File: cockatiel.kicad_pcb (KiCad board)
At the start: 4 copper layers, 38 parts, among them J1 Programmer, J10 LED1_EXT, J11 LED1_SEL, J12 LED0_EXT, J13 LED0_SEL, J14 I/O Debug, J15 MIC_P_BYPASS, J16 MIC_N_BYPASS, J17 MIC_P_SEL, J18 MIC_N_SEL, J19 Cox Box Mic In, J20 Cox Box Mic Out, J21 Microphone out, J22 Headset Socket, J3 DEBUG_UART, J4 RESET, J5 Magnetic connector, J6 PANEL_POWER_BUTTON (MFB), J7 Battery Connector, J8 LED2_EXT, J9 LED2_SEL, U1 F-3188_CSR8645

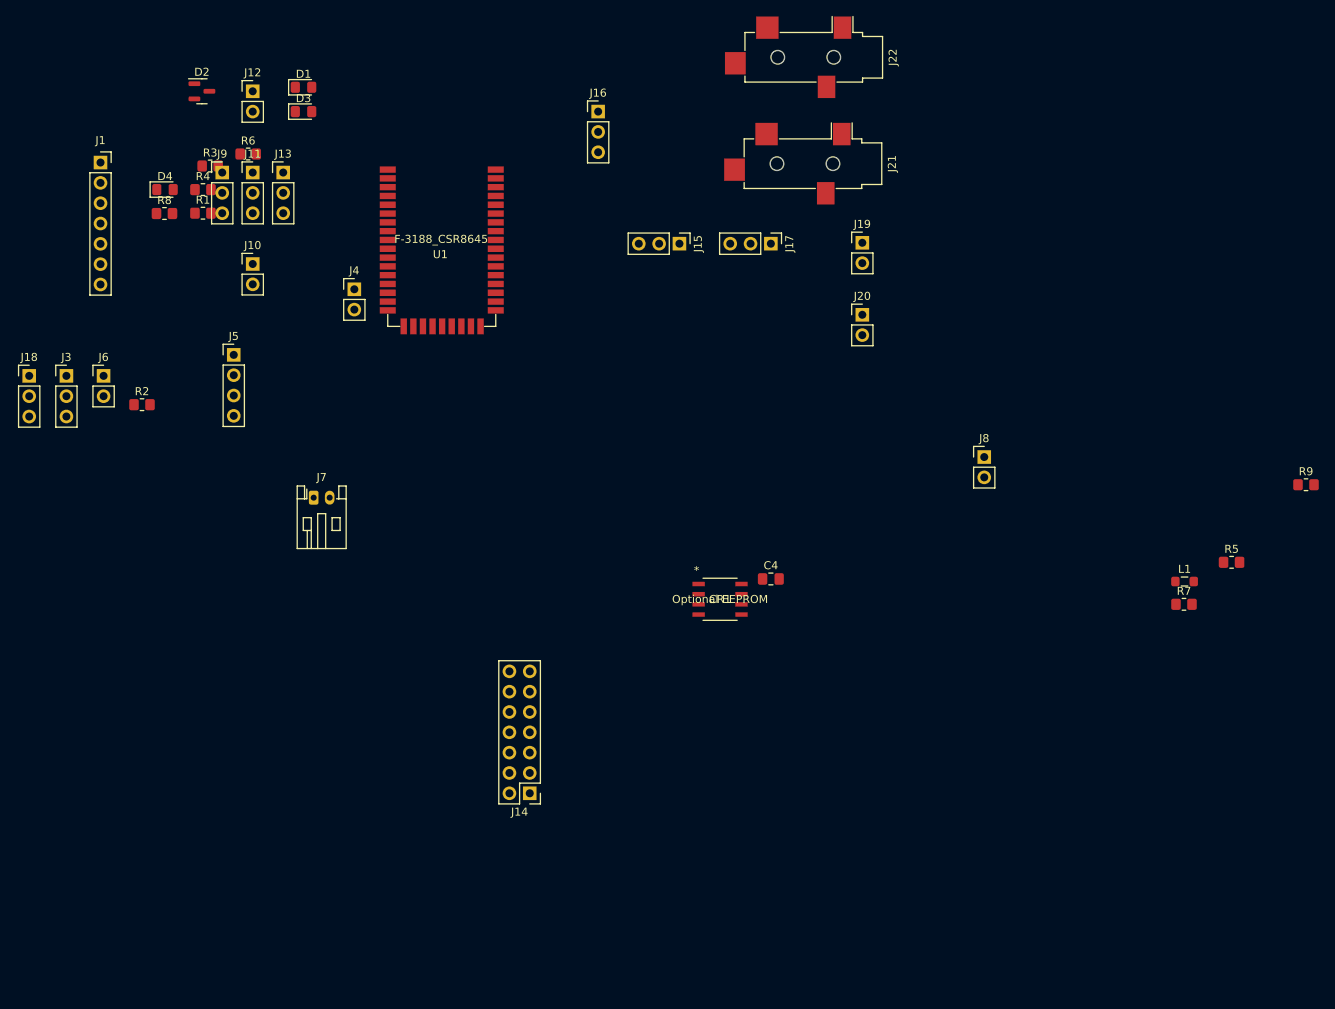
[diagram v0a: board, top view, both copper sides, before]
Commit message: WIP
1. Add transformer footprint.
2. PCB routing
3. Misc changes to re-add JLCPCB part numbers.
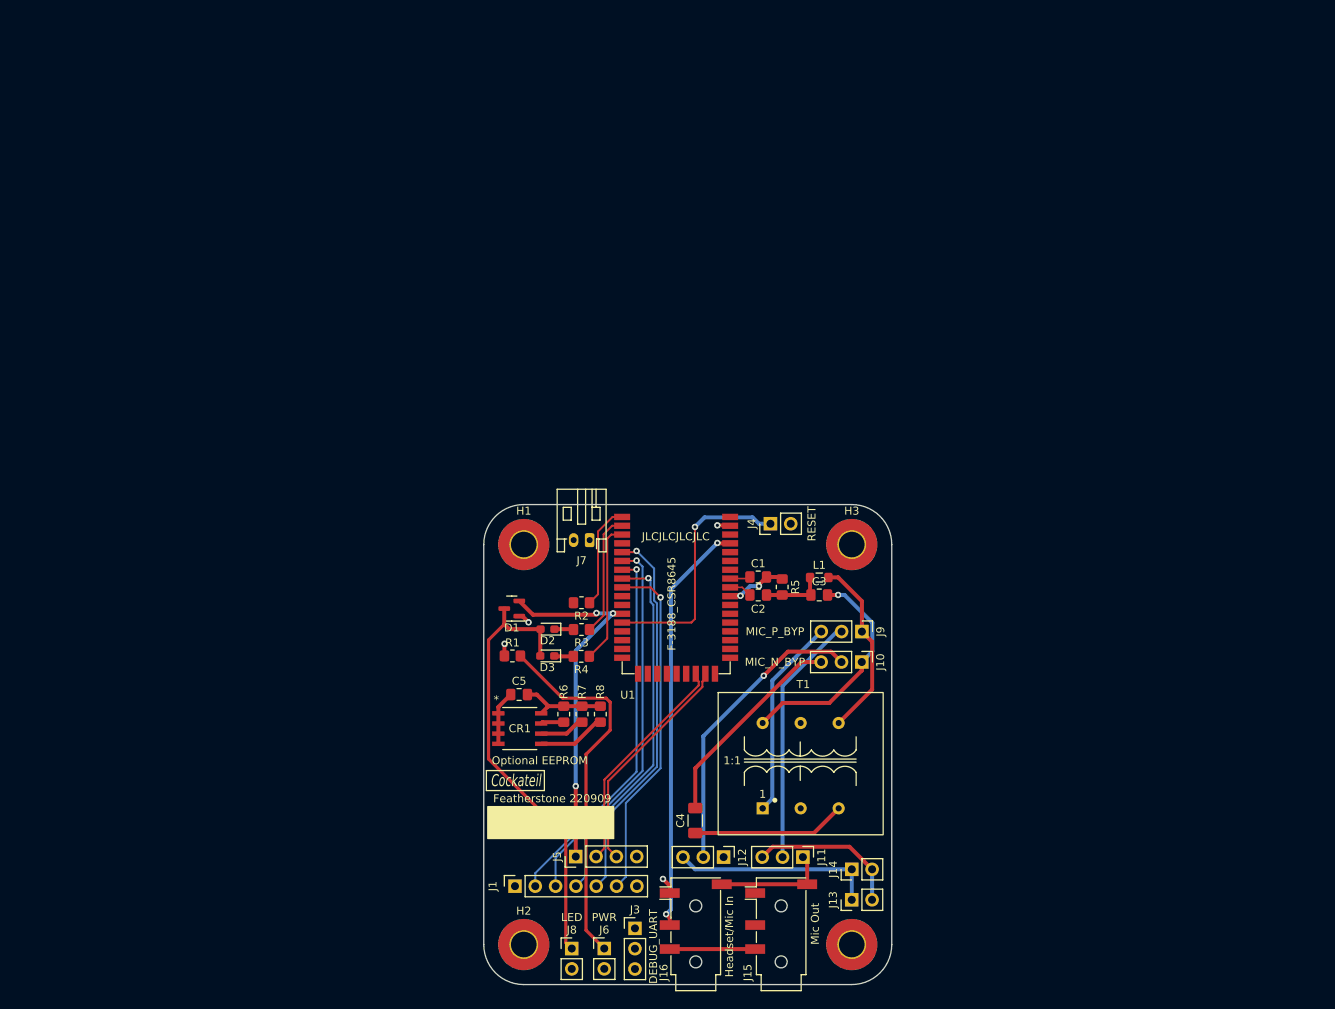
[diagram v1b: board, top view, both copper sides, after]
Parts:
- removed the D1 at (77.5, 52.8)
- removed the J10 at (71.1, 74.9)
- removed the J11 at (71.1, 63.5)
- removed the J12 at (71.1, 53.3)
- removed the J13 at (74.9, 63.5)
- removed the J14 at (105.8, 141.1)
- removed the J9 at (67.3, 63.5)
- removed the R2 at (57.3, 92.5)
- removed the R3 at (65.8, 62.7)
- removed the R4 at (64.9, 65.6)
- removed the R5 at (193.5, 112.2)
- added C1: 100n, Capacitor_SMD:C_0805_2012Metric_Pad1.18x1.45mm_HandSolder, F.Cu at (134.3, 114.1)
- added C2: 100n, Capacitor_SMD:C_0805_2012Metric_Pad1.18x1.45mm_HandSolder, F.Cu at (134.3, 116.3)
- added C3: 15p, Capacitor_SMD:C_0805_2012Metric_Pad1.18x1.45mm_HandSolder, F.Cu at (141.9, 116.3)
- added C4: 22u, Capacitor_SMD:C_1206_3216Metric_Pad1.33x1.80mm_HandSolder, F.Cu at (126.4, 144.5)
- added H1: MountingHole_Pad, MountingHole:MountingHole_3.2mm_M3_Pad_TopBottom, F.Cu at (105.0, 110.0)
- added H2: MountingHole_Pad, MountingHole:MountingHole_3.2mm_M3_Pad_TopBottom, F.Cu at (105.0, 160.0)
- added H3: MountingHole_Pad, MountingHole:MountingHole_3.2mm_M3_Pad_TopBottom, F.Cu at (146.0, 110.0)
- added H4: MountingHole_Pad, MountingHole:MountingHole_3.2mm_M3_Pad_TopBottom, F.Cu at (146.0, 160.0)
- added R6: 2K2, Resistor_SMD:R_0805_2012Metric_Pad1.20x1.40mm_HandSolder, F.Cu at (110.0, 131.2)
- added R7: 2K2, Resistor_SMD:R_0805_2012Metric_Pad1.20x1.40mm_HandSolder, F.Cu at (112.3, 131.2)
- added R8: 2K2, Resistor_SMD:R_0805_2012Metric_Pad1.20x1.40mm_HandSolder, F.Cu at (114.6, 131.2)
- added T1: Transformer_Audio, cockateil:Transformer_Triad_T Y-141PN, F.Cu at (134.9, 143.0)
- D2: renamed from D3; footprint LED_SMD:LED_0805_2012Metric_Pad1.15x1.40mm_HandSolder -> LED_SMD:LED_0603_1608Metric_Pad1.05x0.95mm_HandSolder
- D3: renamed from D4; footprint LED_SMD:LED_0805_2012Metric_Pad1.15x1.40mm_HandSolder -> LED_SMD:LED_0603_1608Metric_Pad1.05x0.95mm_HandSolder
- J10: renamed from J16; value MIC_N_BYPASS -> MIC_N_BYP
- J15: renamed from J21; value Microphone out -> Mic Out; footprint Connector_Audio:Jack_3.5mm_CUI_SJ-3524-SMT_Horizontal -> Connector_Audio:Jack_3.5mm_PJ320D_Horizontal
- J16: renamed from J22; value Headset Socket -> Headset/Mic In; footprint Connector_Audio:Jack_3.5mm_CUI_SJ-3524-SMT_Horizontal -> Connector_Audio:Jack_3.5mm_PJ320D_Horizontal
- J6: value PANEL_POWER_BUTTON (MFB) -> PWR
- J8: value LED2_EXT -> LED
- J9: renamed from J15; value MIC_P_BYPASS -> MIC_P_BYP
- moved J16 109.3 mm to (126.5, 157.4), turned to 90 degrees
- moved J12 105.6 mm to (130.0, 149.1), turned to -90 degrees
- moved J1 104.2 mm to (103.9, 152.7), turned to 90 degrees
- moved J3 99.1 mm to (118.9, 158.0)
- moved J15 95.1 mm to (137.2, 157.4), turned to 90 degrees
- moved J6 95.1 mm to (115.1, 160.5)
- moved J13 82.1 mm to (146.0, 154.4), turned to 90 degrees
- moved J8 80.2 mm to (111.0, 160.5)
- moved J11 76.8 mm to (139.9, 149.1)
- moved J10 76.3 mm to (147.3, 124.7), turned to -90 degrees
- moved R4 76.0 mm to (112.2, 124.0), turned to 180 degrees
- moved J5 75.9 mm to (111.5, 149.0), turned to 90 degrees
- moved D3 75.4 mm to (107.9, 123.9), turned to 180 degrees
- moved R3 75.4 mm to (112.2, 120.6), turned to 180 degrees
- moved D1 75.4 mm to (103.5, 118.0), turned to 180 degrees
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- renumbered C4 to C5, D2 to D1, J17 to J11, J18 to J12, J19 to J13, J20 to J14, R6 to R2, R7 to R3, R8 to R4, R9 to R5
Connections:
- C5 pad 1: +1V8 -> Earth
- C5 pad 2: Earth -> +1V8
- D2 pad 1: Net-(D3-Pad1) -> Net-(D2-Pad1)
- D3 pad 1: Net-(D4-Pad1) -> Net-(D3-Pad1)
- J12 pad 1: GND -> Earth
- J5 pad 2: Net-(J5-Pad2) -> USB_N
- J5 pad 3: Net-(J5-Pad3) -> USB_P
- R2 pad 1: Net-(J9-Pad2) -> /LED2
- R2 pad 2: /LED2 -> Net-(J8-Pad2)
- R3 pad 1: Net-(J11-Pad2) (its old number) -> /LED1
- R3 pad 2: /LED1 -> Net-(D2-Pad1)
- R4 pad 1: Net-(J13-Pad2) -> /LED0
- R4 pad 2: /LED0 -> Net-(D3-Pad1)
- U1 pad 43: GND -> Earth
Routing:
- net Net-(D1-Pad3): track 0.00 -> 55.8 mm
- net /SPK_R: track 0.00 -> 52.2 mm, vias 0 -> 2
- net /MISO: track 0.00 -> 48.0 mm, vias 0 -> 1
- net /~{CS}: track 0.00 -> 47.4 mm, vias 0 -> 1
- net /SPI_CLK: track 0.00 -> 46.8 mm, vias 0 -> 1
- net Net-(J6-Pad1): track 0.00 -> 46.6 mm
- net /MOSI: track 0.00 -> 46.6 mm, vias 0 -> 1
- net VBUS: track 0.00 -> 46.4 mm, vias 0 -> 3
- net /SPI_EN: track 0.00 -> 43.7 mm, vias 0 -> 1
- net Net-(J10-Pad2): track 0.00 -> 37.3 mm, vias 0 -> 1
- net Net-(J11-Pad2): track 0.00 -> 31.6 mm
- net /~{RST}: track 0.00 -> 31.1 mm, vias 0 -> 1
- net Net-(C3-Pad2): track 0.00 -> 28.7 mm, vias 0 -> 1
- net USB_N: track 0.00 -> 28.3 mm
- net USB_P: track 0.00 -> 28.3 mm
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- added copper zone on In2.Cu, net +BATT
- added copper zone on In1.Cu, net Earth
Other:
- board outline added: 51 x 60 mm
- board text added: "Cockateil"
- board text added: "Featherstone 220909"
- board text added: "JLCJLCJLCJLC"

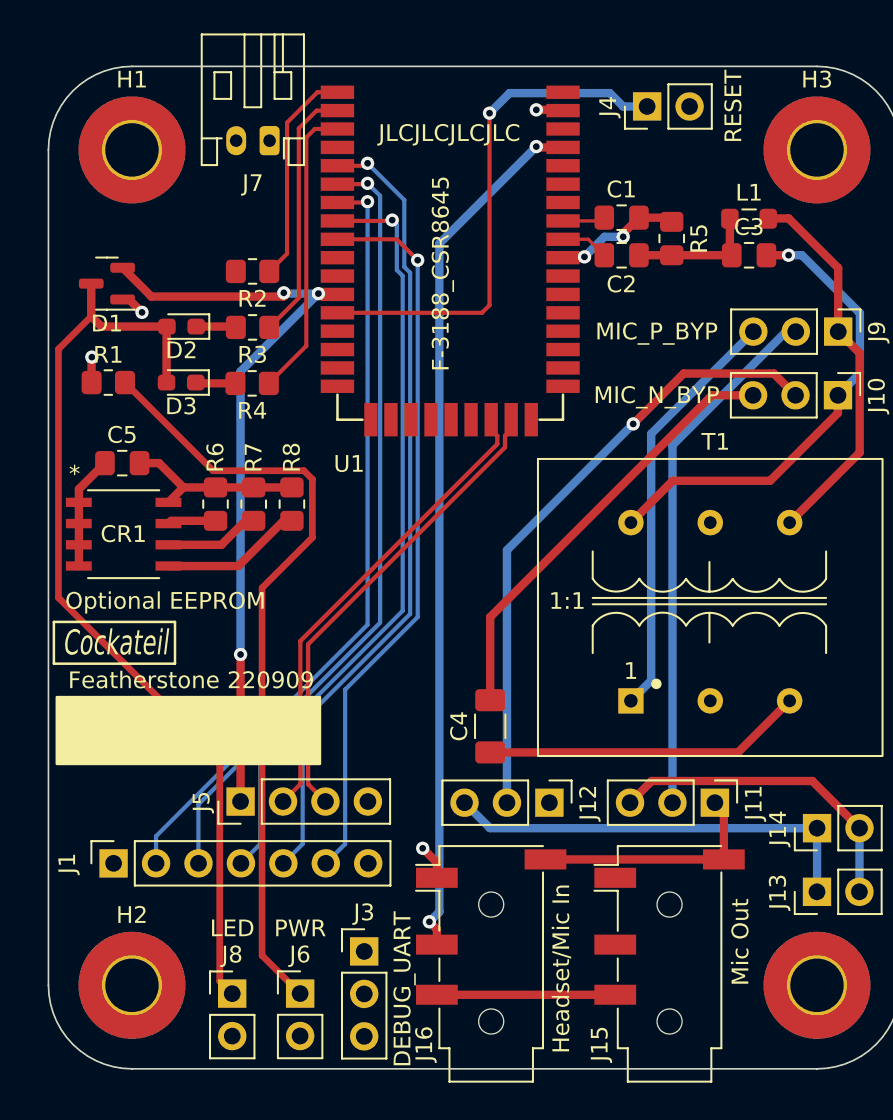
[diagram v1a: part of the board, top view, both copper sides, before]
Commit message: Complete board layout and JLCPCB component allocation.
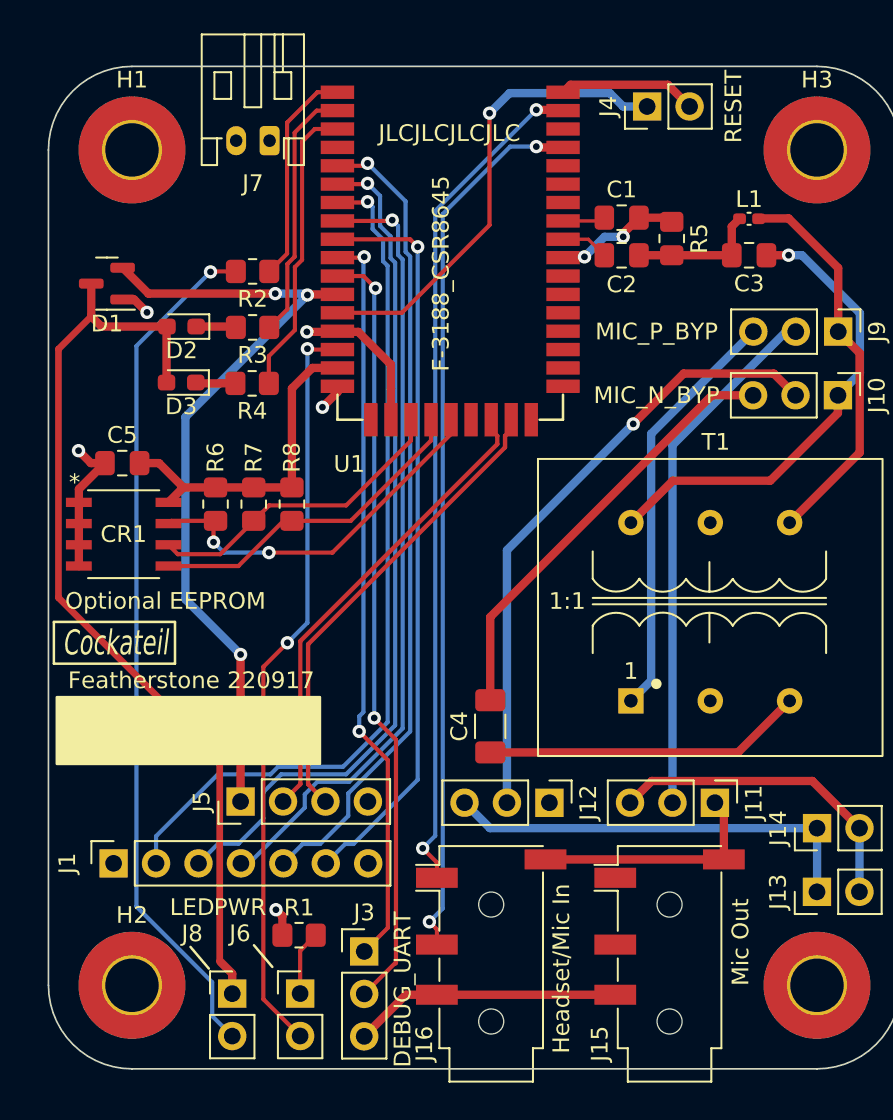
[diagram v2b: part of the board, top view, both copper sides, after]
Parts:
- L1: footprint Inductor_SMD:L_0805_2012Metric_Pad1.05x1.20mm_HandSolder -> Inductor_SMD:L_0402_1005Metric_Pad0.77x0.64mm_HandSolder
- moved R1 35.0 mm to (115.0, 157.0)
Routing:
- net Net-(J8-Pad2): track 0.00 -> 51.5 mm, vias 0 -> 1
- net /SPK_L: track 3.74 -> 50.8 mm
- net BT_UART_RX: track 0.00 -> 46.3 mm, vias 0 -> 2
- net /POWER_EN: track 0.00 -> 45.0 mm, vias 0 -> 2
- net BT_UART_TX: track 0.02 -> 44.6 mm, vias 0 -> 2
- net Net-(J6-Pad1): track 46.6 -> 3.88 mm
- net /PIO12: track 2.89 -> 22.5 mm, vias 0 -> 2
- net Earth: track 17.5 -> 34.7 mm, vias 0 -> 2
- net /PIO10: track 5.70 -> 18.8 mm
- net /PIO11: track 8.51 -> 20.1 mm
- net +1V8: track 11.0 -> 20.1 mm
- net +BATT: track 3.60 -> 12.6 mm, vias 2 -> 3
- net /SPI_CLK: track 46.8 -> 51.8 mm
- net /~{CS}: track 47.4 -> 51.1 mm
- net /~{RST}: track 31.1 -> 28.2 mm
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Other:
- board text added: "Featherstone 220917"
- board text removed: "Featherstone 220909"

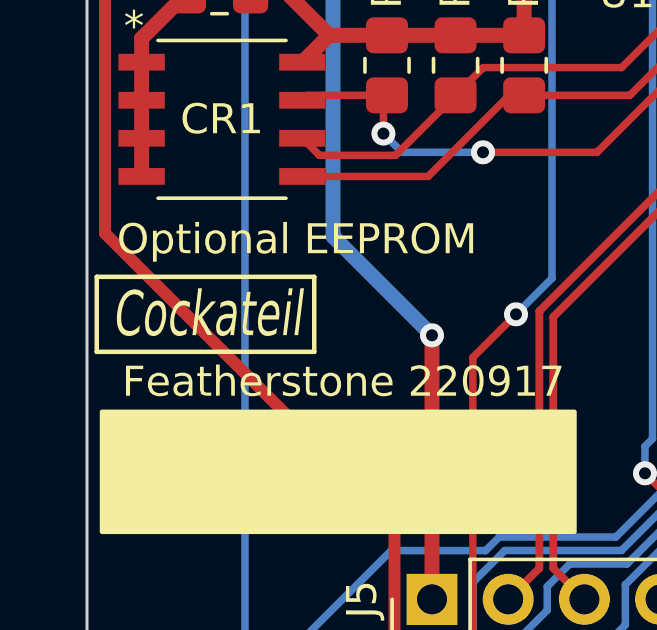
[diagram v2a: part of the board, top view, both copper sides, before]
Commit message: Correct typo
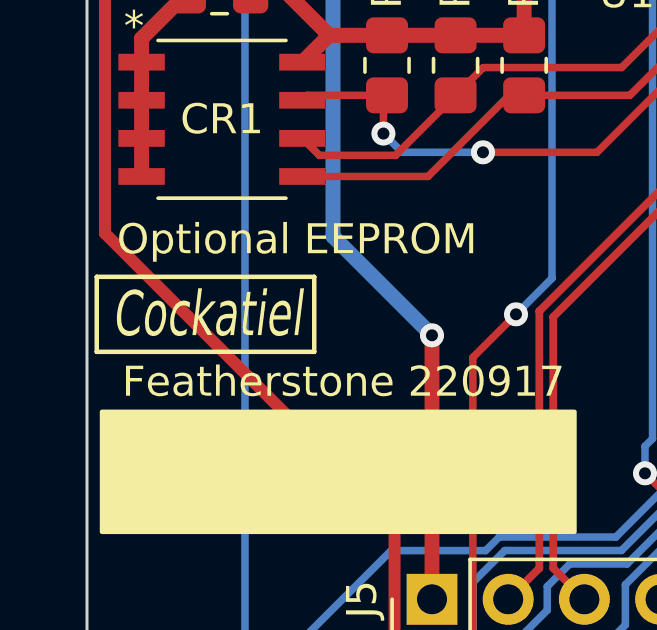
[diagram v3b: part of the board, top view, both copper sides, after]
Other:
- board text added: "Cockatiel"
- board text removed: "Cockateil"
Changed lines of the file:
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@@
     (effects (font (size 1 1) (thickness 0.15)))
   )
-  (gr_text "Cockateil" (at 104.002381 139.5) (layer "F.SilkS")
+  (gr_text "Cockatiel" (at 104.002381 139.5) (layer "F.SilkS")
     (effects (font (size 1.5 1) (thickness 0.25) italic))
   )

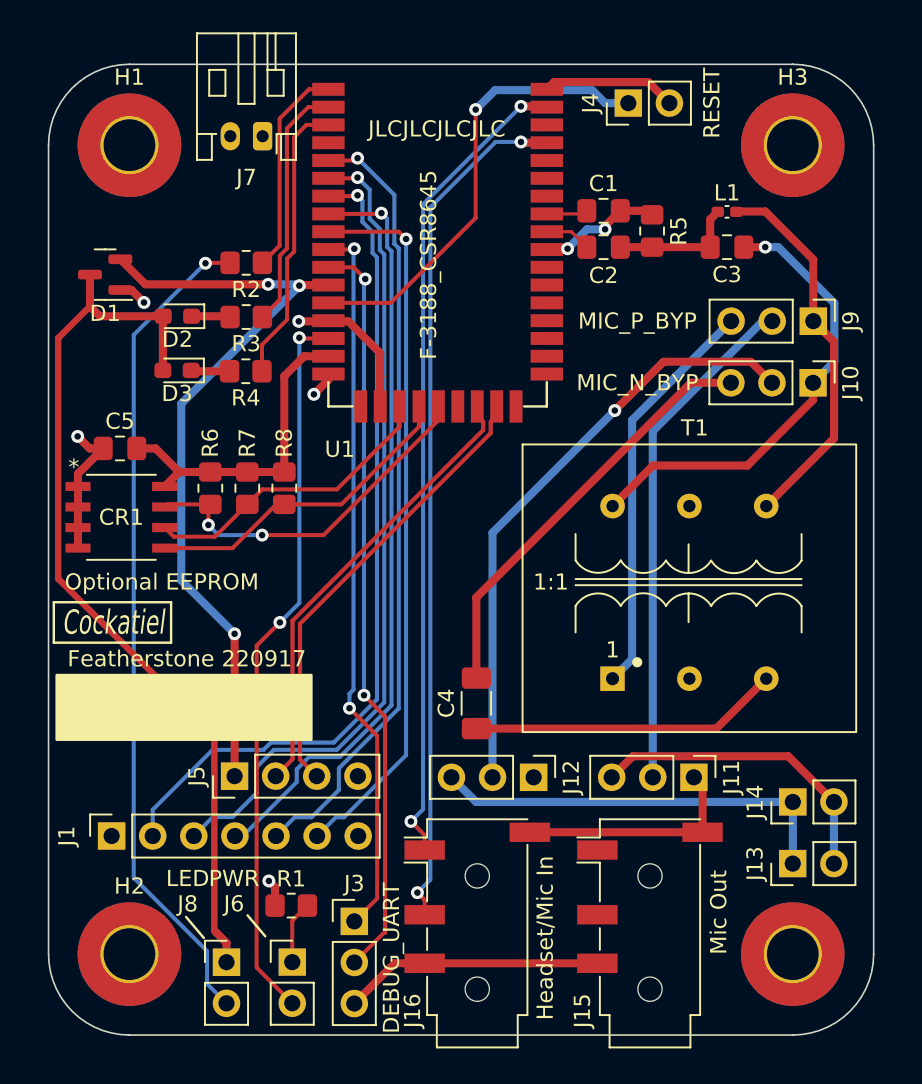
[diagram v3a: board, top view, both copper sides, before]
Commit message: Several improvements to board layout:
1. Fill front and back copper with ground pour.
2. Add information about the product into the back copper.
3. Add cockatiel logo to the silkscreen.
4. Update build date string/version.
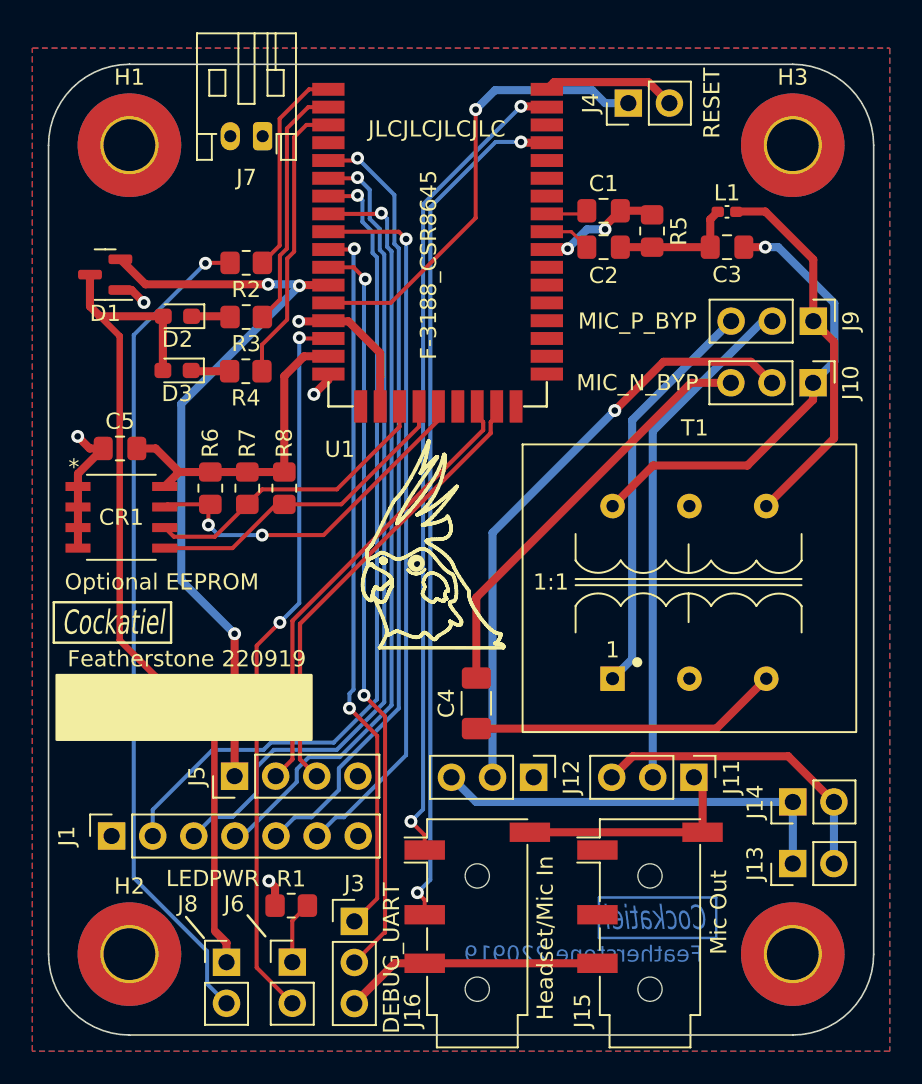
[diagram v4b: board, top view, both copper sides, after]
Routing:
- net Net-(D1-Pad3): track 55.8 -> 54.1 mm
- added copper zone on B.Cu, net Earth
- added copper zone on F.Cu, net Earth
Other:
- board text added: "Featherstone 220919"
- board text removed: "Featherstone 220917"
